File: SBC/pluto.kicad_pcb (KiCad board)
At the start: 4 copper layers, 64 parts, among them J1 VCC1, J10 GND3, J11 Expansion Bus, J12 VIA2PB, J2 GND1, J3 VCC2, J4 POWER, J5 GND2, J6 RS232a, J7 RS232b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

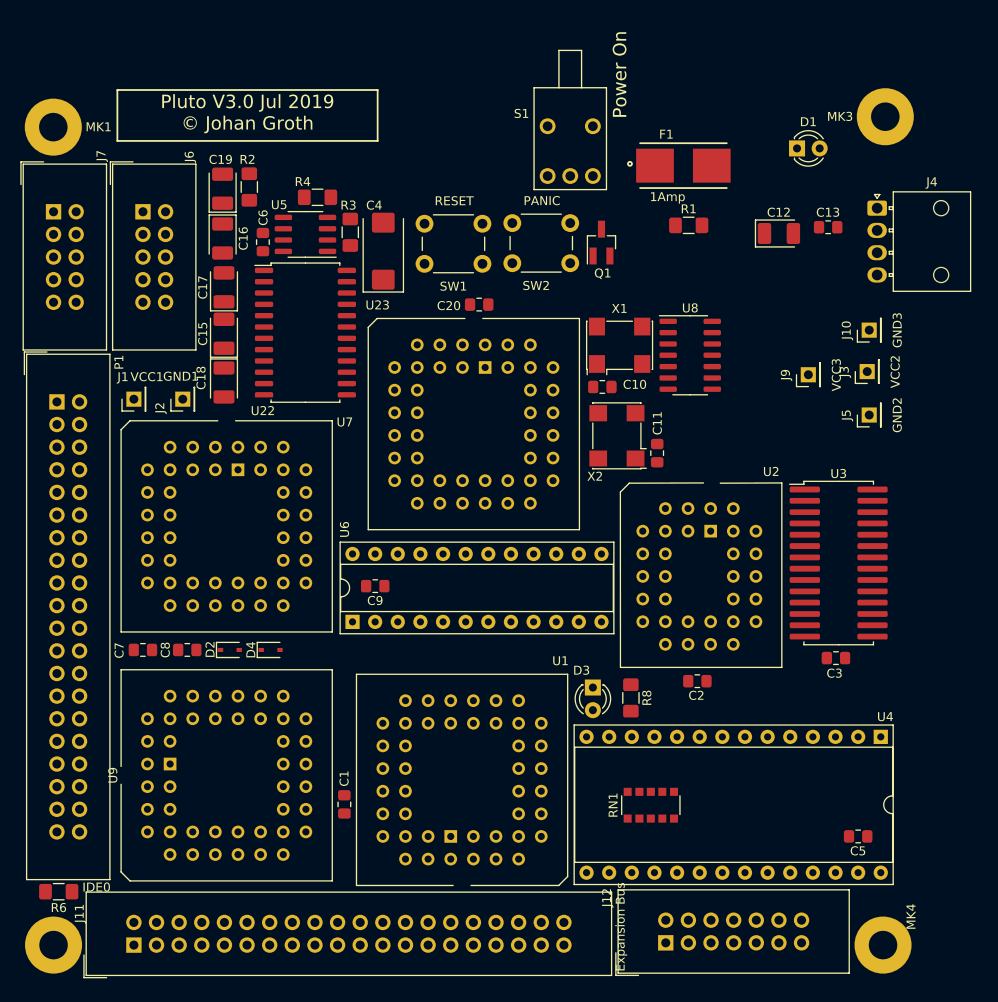
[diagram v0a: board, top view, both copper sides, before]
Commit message: Added de-coupling cap to 74hc74. Rearranged PCB a bit.
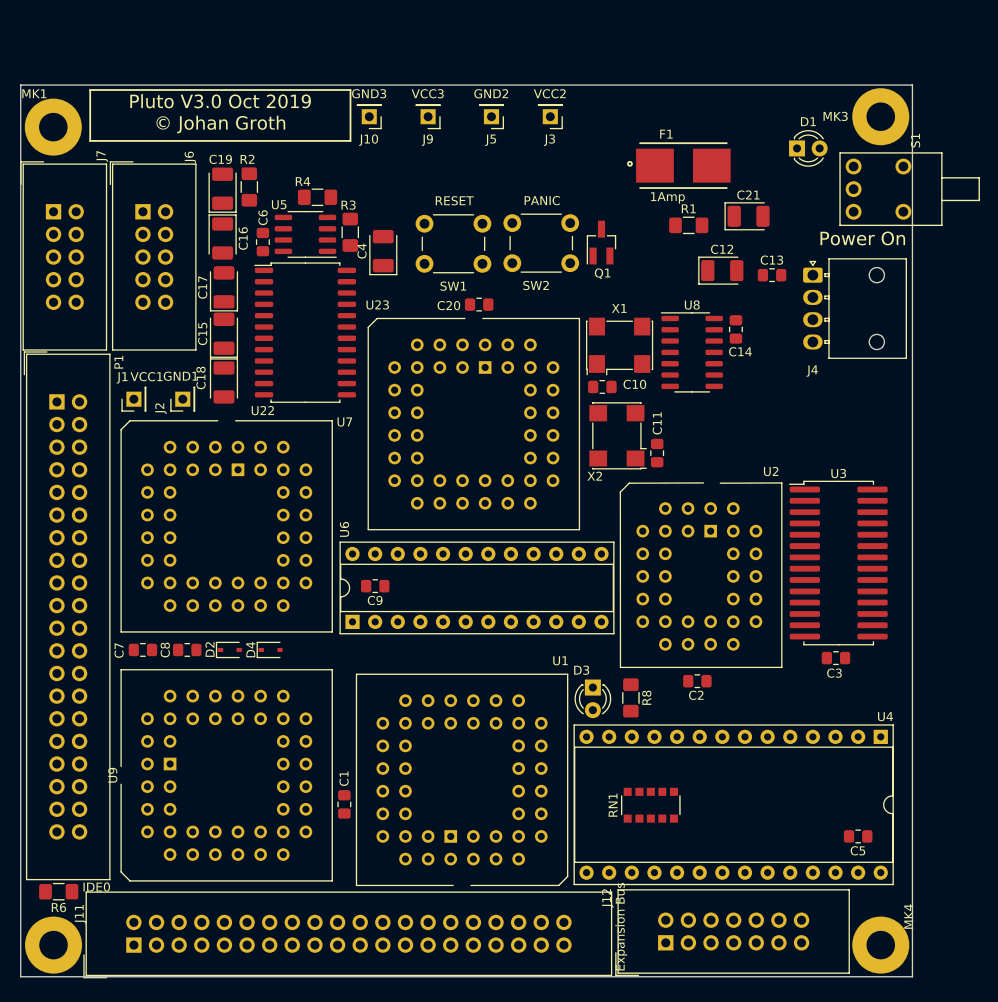
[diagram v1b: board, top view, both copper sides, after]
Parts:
- added C14: 0.1uF, Capacitor_SMD:C_0805_2012Metric_Pad1.15x1.40mm_HandSolder, F.Cu at (135.0, 67.6)
- added C21: 100uF, Capacitor_Tantalum_SMD:CP_EIA-3528-15_AVX-H_Pad1.50x2.35mm_HandSolder, F.Cu at (136.4, 54.9)
- C4: footprint Capacitor_Tantalum_SMD:CP_EIA-7343-31_Kemet-D_Pad2.25x2.55mm_HandSolder -> Capacitor_Tantalum_SMD:CP_EIA-3528-15_AVX-H_Pad1.50x2.35mm_HandSolder
- U3: footprint Package_SO:SOJ-28_7.585x18.12mm_P1.27mm -> Grotto:SOJ-28_7.585x18.12mm_P1.27mm
- X1: value 8MHz -> 16MHz
- moved J10 61.0 mm to (93.9, 43.7), turned to 180 degrees
- moved J5 54.0 mm to (107.6, 43.7), turned to 180 degrees
- moved J9 51.6 mm to (100.5, 43.7), turned to 180 degrees
- moved J3 45.6 mm to (114.2, 43.7), turned to 180 degrees
- moved S1 35.1 mm to (151.3, 51.8), turned to 270 degrees
- moved J4 10.4 mm to (143.6, 61.5)
- moved C13 8.28 mm to (139.1, 61.5)
- moved C12 7.60 mm to (133.5, 61.0)
- moved MK3 0.51 mm to (151.3, 43.7)
- moved U8 0.39 mm to (130.1, 70.1)
- moved MK4 0.25 mm to (151.3, 136.7)
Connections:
- U8 pad 1: GND -> VCC
- U8 pad 10: VCC -> GND
- U8 pad 11: Net-(U8-Pad11) -> GND
- U8 pad 12: Net-(U8-Pad12) -> GND
- U8 pad 13: VCC -> GND
- U8 pad 2: GND -> Net-(U8-Pad2)
- U8 pad 3: GND -> Net-(U8-Pad3)
- U8 pad 4: GND -> VCC
- U8 pad 5: Net-(U8-Pad5) -> /16bit IDE interface/CLK
- U8 pad 6: Net-(U8-Pad6) -> Net-(U8-Pad2)
- U8 pad 8: Net-(U8-Pad12) -> Net-(U8-Pad8)
- U8 pad 9: /16bit IDE interface/CLK -> Net-(U8-Pad9)
- X1 pad 3: Net-(U8-Pad11) -> Net-(U8-Pad3)
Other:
- board outline added: 100.1 x 100.1 mm
- board text added: "Pluto V3.0 Oct 2019 © Johan Groth"
- board text removed: "Pluto V3.0 Jul 2019 © Johan Groth"

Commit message: Pluto2 V3 PCB routed and finished. Removed all Pluto2 V2 Gerber files. Add GAL files for address and IO decoding.
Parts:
- D2, D4: footprint Diode_SMD:D_SOD-323 -> Diode_SMD:D_SOD-323_HandSoldering
- moved J1 67.8 mm to (127.4, 43.7)
- moved J2 57.4 mm to (120.8, 43.7)
- moved R4 49.5 mm to (134.5, 69.9), turned to 90 degrees
- moved C6 46.1 mm to (127.6, 63.8), turned to 0 degrees
- moved R2 45.8 mm to (124.3, 64.5), turned to 270 degrees
- moved U5 44.0 mm to (129.3, 67.7), turned to 0 degrees
- moved R3 35.2 mm to (124.3, 69.8)
- moved C4 27.9 mm to (121.3, 69.2)
- moved C2 23.7 mm to (131.2, 83.3)
- moved SW1 21.8 mm to (128.3, 58.9)
- moved C19 18.7 mm to (93.9, 60.6)
- moved C14 17.6 mm to (151.0, 74.9)
- moved U8 17.6 mm to (146.1, 77.5)
- moved C10 17.5 mm to (136.0, 81.1)
- moved X1 17.5 mm to (137.9, 76.5)
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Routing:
- net /16bit IDE interface/~RES: track 0.00 -> 214.6 mm, vias 0 -> 1
- net /16bit IDE interface/A2: track 0.00 -> 197.1 mm, vias 0 -> 1
- net /16bit IDE interface/A0: track 0.00 -> 195.6 mm
- net /16bit IDE interface/A1: track 0.00 -> 195.3 mm
- net /Address decoding and support section/~MWR: track 0.00 -> 186.3 mm, vias 0 -> 1
- net /16bit IDE interface/D4: track 0.00 -> 186.2 mm
- net /16bit IDE interface/D6: track 0.00 -> 179.9 mm, vias 0 -> 1
- net /16bit IDE interface/A3: track 0.00 -> 179.4 mm, vias 0 -> 2
- net /16bit IDE interface/D7: track 0.00 -> 176.3 mm
- net /16bit IDE interface/D5: track 0.00 -> 175.8 mm
- net /16bit IDE interface/D0: track 0.00 -> 175.6 mm
- net /16bit IDE interface/D3: track 0.00 -> 173.0 mm
- net /16bit IDE interface/D2: track 0.00 -> 172.5 mm
- net /Address decoding and support section/~MRD: track 0.00 -> 161.3 mm, vias 0 -> 1
- net /16bit IDE interface/D1: track 0.00 -> 158.3 mm, vias 0 -> 1
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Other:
- board size 100.1 x 100.1 mm -> 99.8 x 99.8 mm

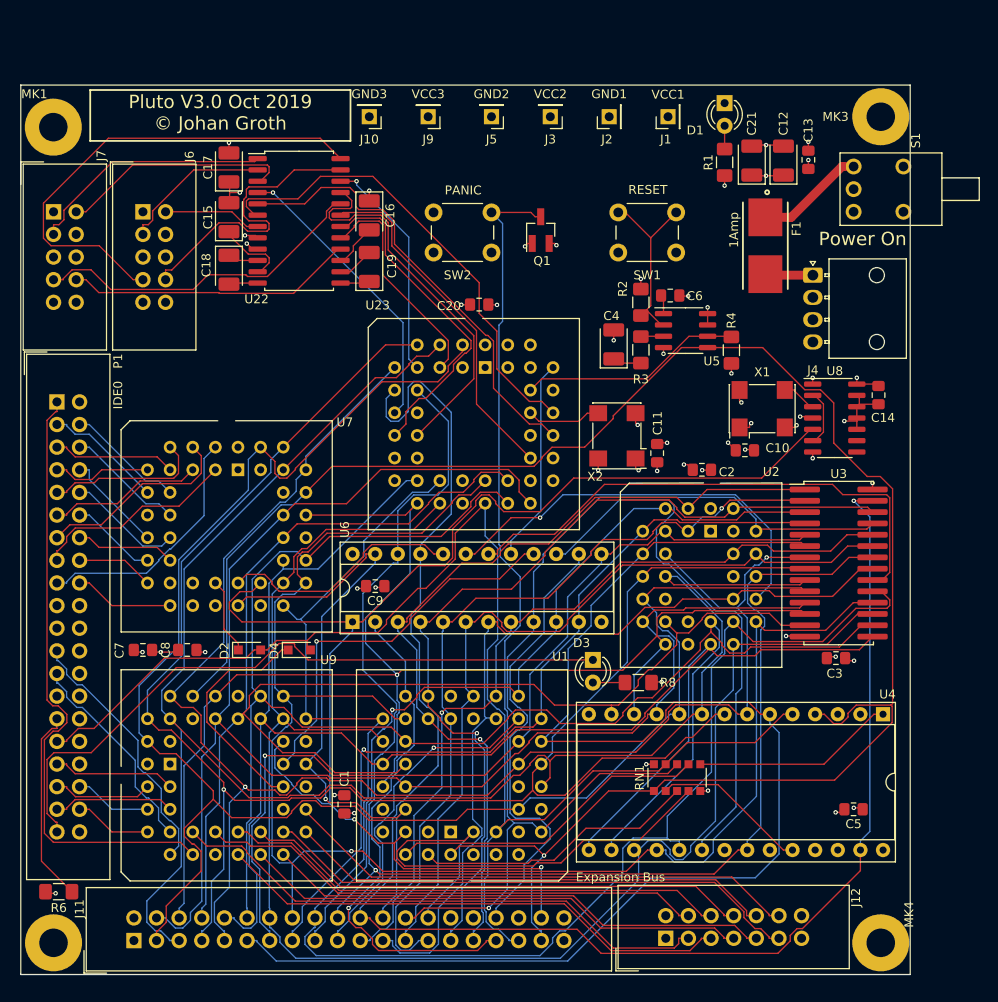
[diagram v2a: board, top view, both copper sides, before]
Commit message: Added clock generator using an Arduino Nano. Gerbers made and sent to manufacturer. Some assembler testing bread board setup
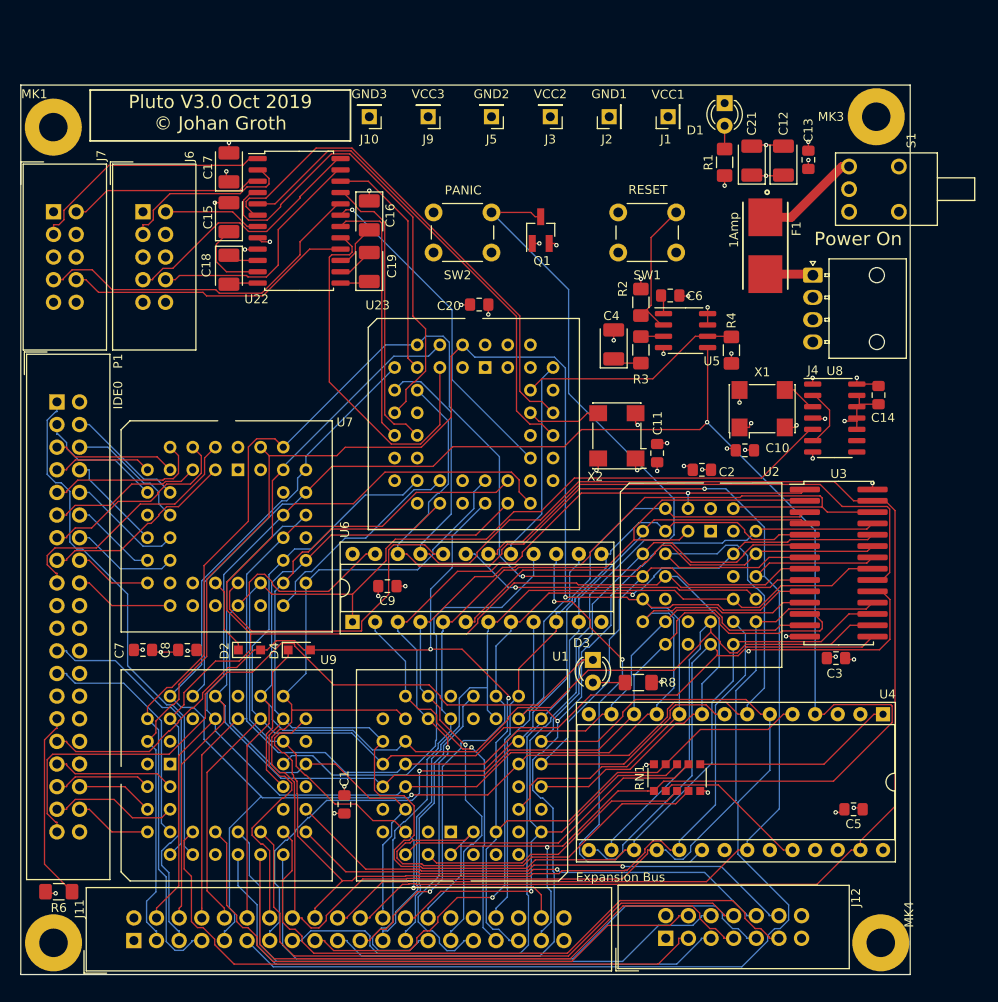
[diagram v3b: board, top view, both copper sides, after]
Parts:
- moved C9 1.36 mm to (95.9, 96.4)
- moved MK3 0.51 mm to (150.7, 43.7)
- moved S1 0.51 mm to (150.7, 51.8)
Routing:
- net VCC: track 79.9 -> 125.2 mm, vias 29 -> 30
- net Net-(J6-Pad7): track 54.3 -> 28.8 mm
- net /16bit IDE interface/D2: track 172.5 -> 151.8 mm
- net Net-(U22-Pad4): track 32.9 -> 53.1 mm, vias 1 -> 0
- net /Address decoding and support section/A8: track 100.9 -> 119.3 mm
- net /DUART and RS232/CTSb: track 25.2 -> 41.7 mm
- net /Address decoding and support section/A15: track 58.2 -> 43.1 mm
- net /16bit IDE interface/CLK: track 152.2 -> 137.4 mm, vias 2 -> 1
- net /Address decoding and support section/~NMI: track 126.0 -> 140.1 mm
- net /16bit IDE interface/~RES: track 214.6 -> 201.4 mm, vias 1 -> 2
- net /Address decoding and support section/~ROMSEL: track 47.1 -> 34.7 mm
- net Net-(J12-Pad11): track 61.0 -> 73.1 mm
- net /16bit IDE interface/A2: track 197.1 -> 208.5 mm
- net Net-(J12-Pad9): track 57.0 -> 68.4 mm
- net /CPU, ROM and RAM/A4: track 155.0 -> 166.3 mm
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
